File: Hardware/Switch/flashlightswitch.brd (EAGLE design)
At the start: 38.1 x 50.8 mm, 11 parts

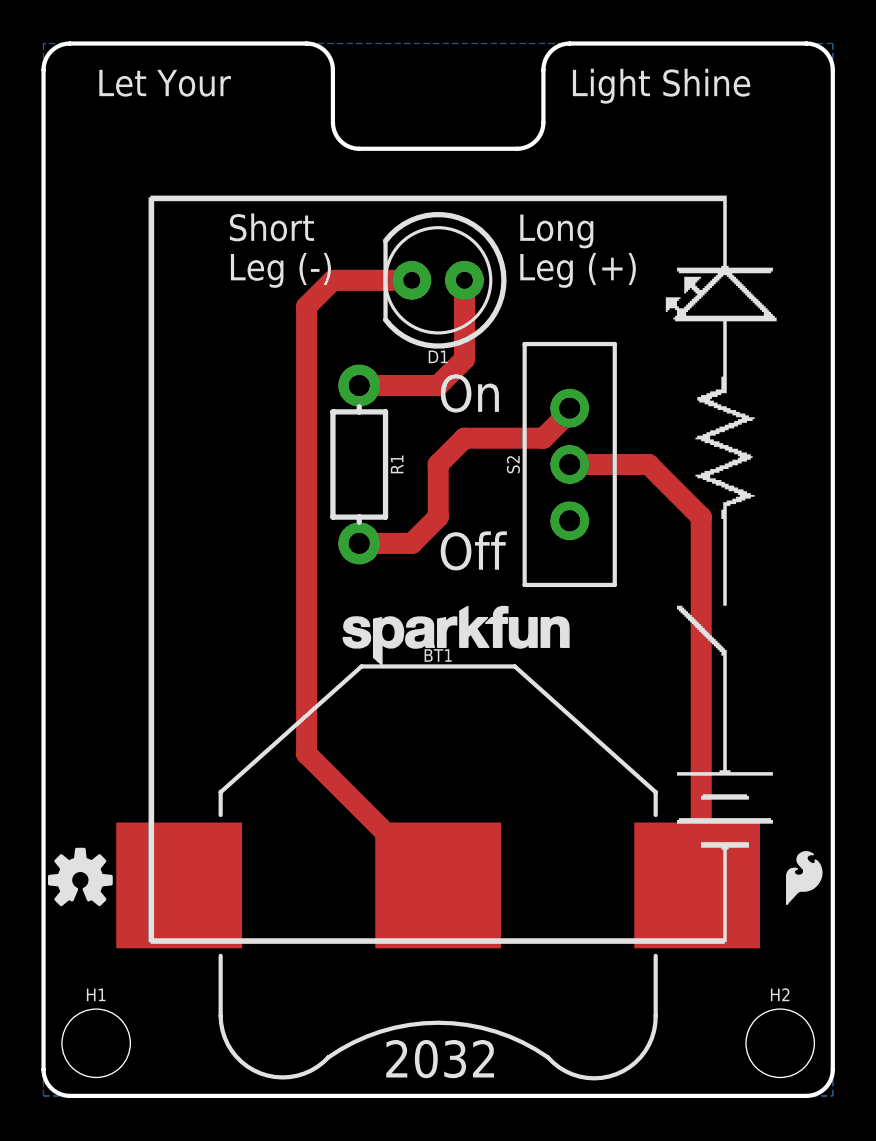
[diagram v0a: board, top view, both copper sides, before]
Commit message: Updated before Proto Review
Made some tweaks to polish up the design a bit before the design review.
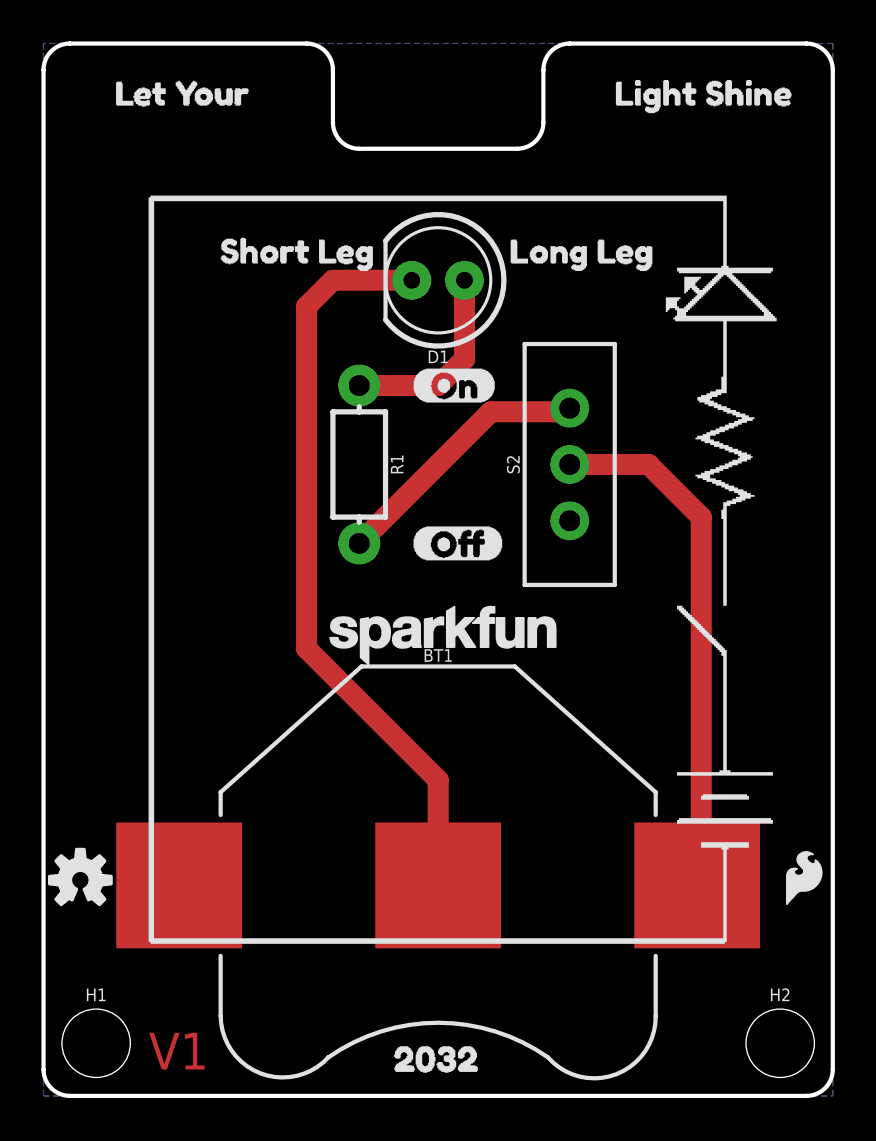
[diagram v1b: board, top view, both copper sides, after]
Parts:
- added LOGO3: SFE_LOGO_NAME_FLAME.2_INCH, SparkFun-Aesthetics:SFE_LOGO_NAME_FLAME_.2
- added U$2: (no value), buzzard_labels:ON0
- added U$3: (no value), buzzard_labels:OFF0
- added U$4: (no value), buzzard_labels:20320
- added U$5: (no value), buzzard_labels:LIGHT_SHINE0
- added U$6: (no value), buzzard_labels:LET_YOUR0
- added U$7: (no value), buzzard_labels:SHORT_LEG0
- added U$8: (no value), buzzard_labels:LONG_LEG0
- moved LOGO4 0.63 mm to (13.3, 20.3)
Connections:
- net N$1 renamed BATT
- net N$4 renamed GND
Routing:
- net N$2: track 14.5 -> 13.0 mm
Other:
- board text added: "Flashlight"
- board text added: "V1"
- board text added: "sparkfun.com/flashlight"
- board text removed: "2032"
- board text removed: "Let Your"
- board text removed: "Light Shine"
- board text removed: "Long Leg (+)"
- board text removed: "Off"
- board text removed: "On"
- board text removed: "Short Leg (-)"
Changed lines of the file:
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@@
 <board>
 <plain>
-<text x="36.83" y="41.91" size="1.27" layer="22" font="vector" ratio="15" rot="MR0" align="top-left">LED (Light
+<text x="36.83" y="40.64" size="1.27" layer="22" font="vector" ratio="15" rot="MR0" align="top-left">LED (Light
 Emitting Diode) -
 This is your
 light.</text>
-<text x="1.27" y="41.91" size="1.27" layer="22" font="vector" ratio="15" rot="MR0" align="top-right">Resistor -
+<text x="1.27" y="34.29" size="1.27" layer="22" font="vector" ratio="15" rot="MR0" align="top-right">Resistor -
 This limits
 the current
 your LED
 recieves</text>
-<text x="25.4" y="22.86" size="1.27" layer="22" font="vector" ratio="15" rot="MR0" align="top-left">Switch - This
+<text x="36.83" y="25.4" size="1.27" layer="22" font="vector" ratio="15" rot="MR0" align="top-left">Switch - This
 completes
 your circuit</text>
@@
 <dimension x1="38.1" y1="0" x2="38.1" y2="50.8" x3="41.91" y3="25.4" textsize="1.27" textratio="15" layer="49" dtype="vertical" unit="inch"/>
 <dimension x1="0" y1="0" x2="38.1" y2="0" x3="19.05" y3="-2.54" textsize="1.27" textratio="15" layer="49" dtype="horizontal" unit="inch"/>
-<text x="8.89" y="39.37" size="1.27" layer="21" font="vector" ratio="15">Short
-Leg (-)</text>
-<text x="22.86" y="39.37" size="1.27" layer="21" font="vector" ratio="15">Long
-Leg (+)</text>
 <wire x1="1.27" y1="50.8" x2="12.7" y2="50.8" width="0.2032" layer="20"/>
 <wire x1="38.1" y1="49.53" x2="36.83" y2="50.8" width="0.2032" layer="20" curve="90"/>
@@
 <wire x1="13.97" y1="49.53" x2="13.97" y2="46.99" width="0.2032" layer="20"/>
 <wire x1="13.97" y1="46.99" x2="15.24" y2="45.72" width="0.2032" layer="20" curve="90"/>
-<text x="2.54" y="48.26" size="1.27" layer="21" font="vector" ratio="15">Let Your</text>
-<text x="25.4" y="48.26" size="1.27" layer="21" font="vector" ratio="15">Light Shine</text>
-<text x="16.383" y="0.889" size="1.778" layer="21" font="vector" ratio="15">2032</text>
-<text x="19.05" y="33.02" size="1.778" layer="21" font="vector" ratio="15">On</text>
-<text x="19.05" y="25.4" size="1.778" layer="21" font="vector" ratio="15">Off</text>
 <wire x1="0" y1="49.53" x2="1.27" y2="50.8" width="0.2032" layer="20" curve="-90"/>
+<text x="31.75" y="43.18" size="1.778" layer="22" rot="MR0">sparkfun.com/flashlight</text>
+<text x="36.83" y="48.26" size="1.778" layer="22" rot="MR0">Flashlight</text>
+<text x="5.08" y="1.27" size="1.778" layer="1">V1</text>
 </plain>
 <attributes>
@@
 <attribute name="SF_SKU" value="COM-00102" x="25.4" y="30.48" size="1.778" layer="27" font="vector" ratio="15" display="off"/>
 </element>
-<element name="LOGO4" library="SparkFun-Aesthetics" package="SFE_LOGO_NAME_.1" value="SFE_LOGO_NAME.1_INCH" x="13.97" y="20.32"/>
+<element name="LOGO4" library="SparkFun-Aesthetics" package="SFE_LOGO_NAME_.1" value="SFE_LOGO_NAME.1_INCH" x="13.335" y="20.32"/>
+<element name="U$3" library="buzzard_labels" package="OFF0" value="" x="17.78" y="26.67"/>
+<element name="U$2" library="buzzard_labels" package="ON0" value="" x="17.78" y="34.29"/>
+<element name="U$4" library="buzzard_labels" package="20320" value="" x="16.002" y="1.778"/>
+<element name="U$5" library="buzzard_labels" package="LIGHT_SHINE0" value="" x="26.67" y="48.26"/>
+<element name="U$6" library="buzzard_labels" package="LET_YOUR0" value="" x="2.54" y="48.26"/>
+<element name="U$7" library="buzzard_labels" package="SHORT_LEG0" value="" x="7.62" y="40.64"/>
+<element name="U$8" library="buzzard_labels" package="LONG_LEG0" value="" x="21.59" y="40.64"/>
+<element name="LOGO3" library="SparkFun-Aesthetics" package="SFE_LOGO_NAME_FLAME_.2" value="SFE_LOGO_NAME_FLAME.2_INCH" x="31.75" y="0" rot="MR0"/>
 </elements>
 <signals>
-<signal name="N$1">
+<signal name="BATT">
 <contactref element="BT1" pad="1"/>
 <contactref element="S2" pad="2"/>
@@
 <contactref element="R1" pad="P$2"/>
 <contactref element="S2" pad="1"/>
-<wire x1="15.24" y1="26.67" x2="17.78" y2="26.67" width="1.016" layer="1"/>
-<wire x1="17.78" y1="26.67" x2="19.05" y2="27.94" width="1.016" layer="1"/>
-<wire x1="19.05" y1="27.94" x2="19.05" y2="30.48" width="1.016" layer="1"/>
-<wire x1="19.05" y1="30.48" x2="20.32" y2="31.75" width="1.016" layer="1"/>
-<wire x1="20.32" y1="31.75" x2="24.13" y2="31.75" width="1.016" layer="1"/>
-<wire x1="24.13" y1="31.75" x2="25.4" y2="33.02" width="1.016" layer="1"/>
 <wire x1="25.4" y1="33.02" x2="25.4" y2="33.1978" width="1.016" layer="1"/>
+<wire x1="15.24" y1="26.67" x2="21.59" y2="33.02" width="1.016" layer="1"/>
+<wire x1="21.59" y1="33.02" x2="25.4" y2="33.02" width="1.016" layer="1"/>
 </signal>
 <signal name="N$3">
@@
 <wire x1="20.32" y1="35.56" x2="20.32" y2="39.37" width="1.016" layer="1"/>
 </signal>
-<signal name="N$4">
+<signal name="GND">
 <contactref element="D1" pad="K"/>
 <contactref element="BT1" pad="2"/>
 <wire x1="19.05" y1="10.16" x2="19.05" y2="12.7" width="0.8128" layer="1"/>
 <wire x1="17.78" y1="39.37" x2="13.97" y2="39.37" width="1.016" layer="1"/>
-<wire x1="13.97" y1="39.37" x2="12.7" y2="38.1" width="1.016" layer="1"/>
-<wire x1="12.7" y1="16.51" x2="19.05" y2="10.16" width="1.016" layer="1"/>
-<wire x1="12.7" y1="38.1" x2="12.7" y2="16.51" width="1.016" layer="1"/>
+<wire x1="12.7" y1="38.1" x2="13.97" y2="39.37" width="1.016" layer="1"/>
+<wire x1="19.05" y1="10.16" x2="19.05" y2="15.24" width="1.016" layer="1"/>
+<wire x1="19.05" y1="15.24" x2="12.7" y2="21.59" width="1.016" layer="1"/>
+<wire x1="12.7" y1="21.59" x2="12.7" y2="38.1" width="1.016" layer="1"/>
 </signal>
 <signal name="N$5">
